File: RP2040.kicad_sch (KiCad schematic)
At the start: 35 parts, among them J201 TYPE-C-31-M-12, SW202 ~{USB_BOOT}, U201 AZ1117R-3.3TRE1, U202 RP2040, U205 W25Q128JVS, Y201 Crystal_GND24

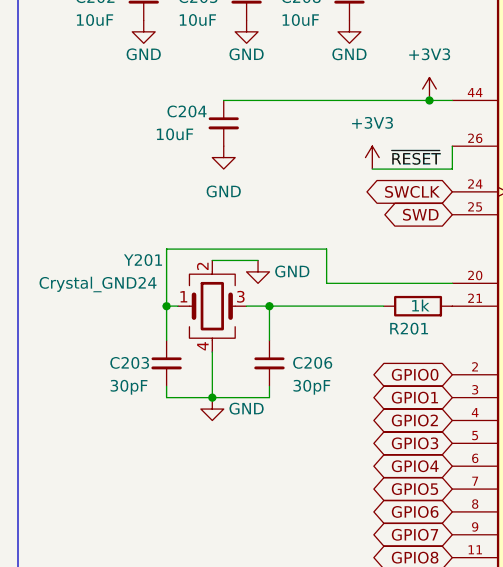
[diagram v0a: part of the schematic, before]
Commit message: Rev 2
Ready to order Rev2:
-Routed missing 1.1V rail
-Swapped LED footprints from 0603 to 0805
-Pins 43 &44 routed to nearest decoupling cap
-Crystal replaced with basic part and created 3D model
-ADC silkscreen improved
-Minor Silkscreen changes
-Generated new gerbers, renders, and PDFs
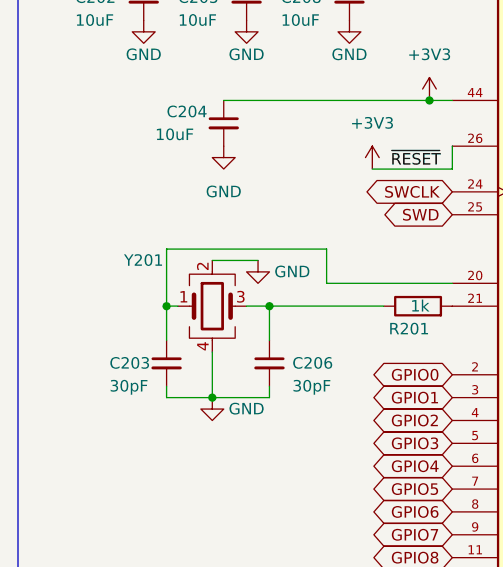
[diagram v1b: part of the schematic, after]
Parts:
- Y201: value Crystal_GND24 -> (none); footprint Breadstick Footprints:7V12000018 -> (none); JLCPCB P/N C97242 -> C9002
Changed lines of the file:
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@@
   (title_block
     (title "RP2040 Template")
-    (date "2022-03-28")
-    (rev "1")
+    (date "2022-04-24")
+    (rev "2")
     (company "J & R Creative Technologies Inc.")
+    (comment 1 "@RangenMichael")
+    (comment 2 "https://twitter.com/RangenMichael")
+    (comment 3 "MIT License")
+    (comment 4 "https://github.com/mrangen/RP2040-Dev-Board")
   )
   (junction (at 110.49 41.91) (diameter 0) (color 0 0 0 0)
@@
     (in_bom yes) (on_board yes)
     (property "Reference" "Y201" (id 0) (at 29.21 72.39 0))
-    (property "Value" "Crystal_GND24" (id 1) (at 24.13 74.93 0))
-    (property "Footprint" "Breadstick Footprints:7V12000018" (id 2) (at 36.83 77.47 0)
+    (property "Value" "" (id 1) (at 24.13 74.93 0))
+    (property "Footprint" "" (id 2) (at 36.83 77.47 0)
       (effects (font (size 1.27 1.27)) hide)
     )
@@
       (effects (font (size 1.27 1.27)) hide)
     )
-    (property "JLCPCB P/N" "C97242" (id 4) (at 36.83 77.47 0)
-      (effects (font (size 1.27 1.27)) hide)
-    )
+    (property "JLCPCB P/N" "C9002" (id 4) (at 36.83 77.47 0)
+      (effects (font (size 1.27 1.27)) hide)
+    )

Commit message: Rev 3
JLCPCB noticed a mistake in my order, I had remnants from an early version in the gerbers folder. Cleared that out and made some updates to the board and resubmitted as Rev3. I added a GND via that was missing near a 3.3V via underneath the RP2040, added Rev 3 to the silkscreen, and nudged C207 away from the USB lines and added a GND via. Gerbers, drill, and centroid files regenerated. Rev 3 renders generated as well.
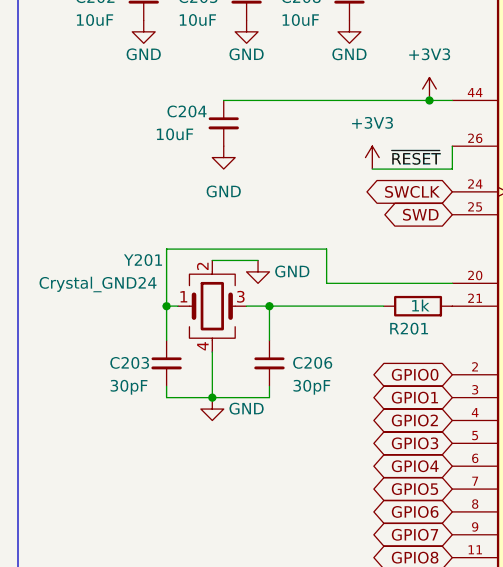
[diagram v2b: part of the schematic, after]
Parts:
- Y201: value (none) -> Crystal_GND24; footprint (none) -> X322516MLB4SI:OSC_X322516MLB4SI
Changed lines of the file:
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@@
   (title_block
     (title "RP2040 Template")
-    (date "2022-04-24")
-    (rev "2")
+    (date "2022-04-25")
+    (rev "3")
     (company "J & R Creative Technologies Inc.")
     (comment 1 "@RangenMichael")
@@
     (in_bom yes) (on_board yes)
     (property "Reference" "Y201" (id 0) (at 29.21 72.39 0))
-    (property "Value" "" (id 1) (at 24.13 74.93 0))
-    (property "Footprint" "" (id 2) (at 36.83 77.47 0)
-      (effects (font (size 1.27 1.27)) hide)
-    )
+    (property "Value" "Crystal_GND24" (id 1) (at 24.13 74.93 0))
+    (property "Footprint" "X322516MLB4SI:OSC_X322516MLB4SI" (id 2) (at 36.83 77.47 0)
+      (effects (font (size 1.27 1.27)) hide)
+    )
